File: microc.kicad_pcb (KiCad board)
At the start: 2 copper layers, 17.8 x 30.5 mm, 17 parts, among them J1 Conn_01x12, J2 Conn_01x12, J3 USB_C_Receptacle_USB2.0, U1 ATmega32U4-AU, U2 USBLC6-2SC6

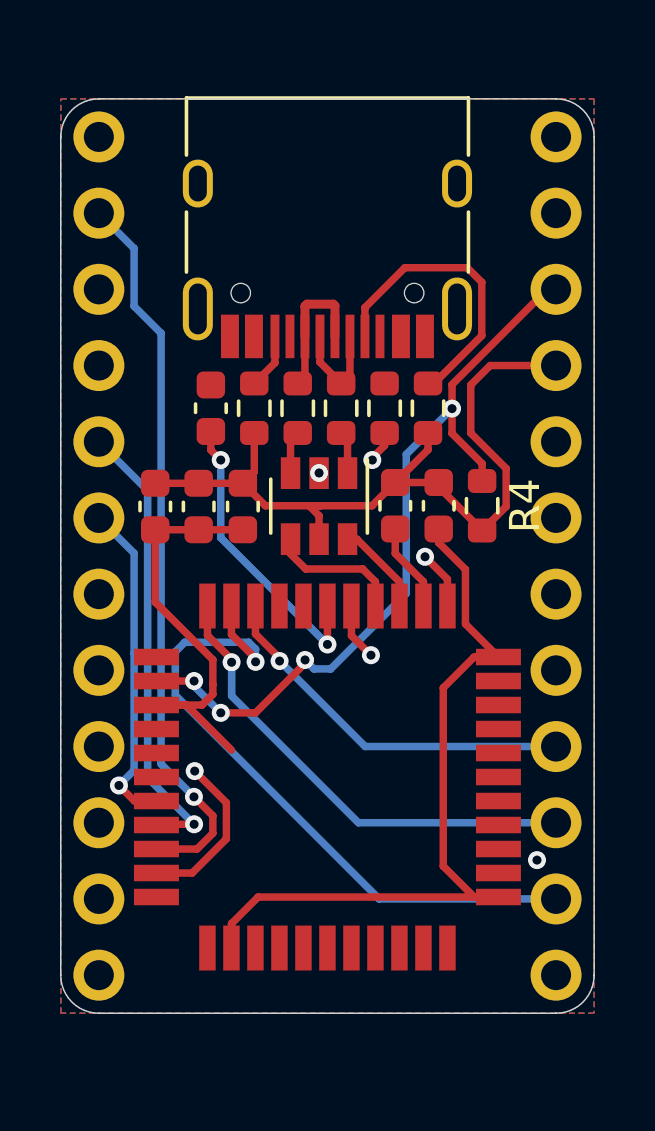
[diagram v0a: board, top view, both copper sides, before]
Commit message: rev 1 - Completed PCB - Completed schematic
Notes:
- Added 0 ohm resistor to schematic in order to help with routing
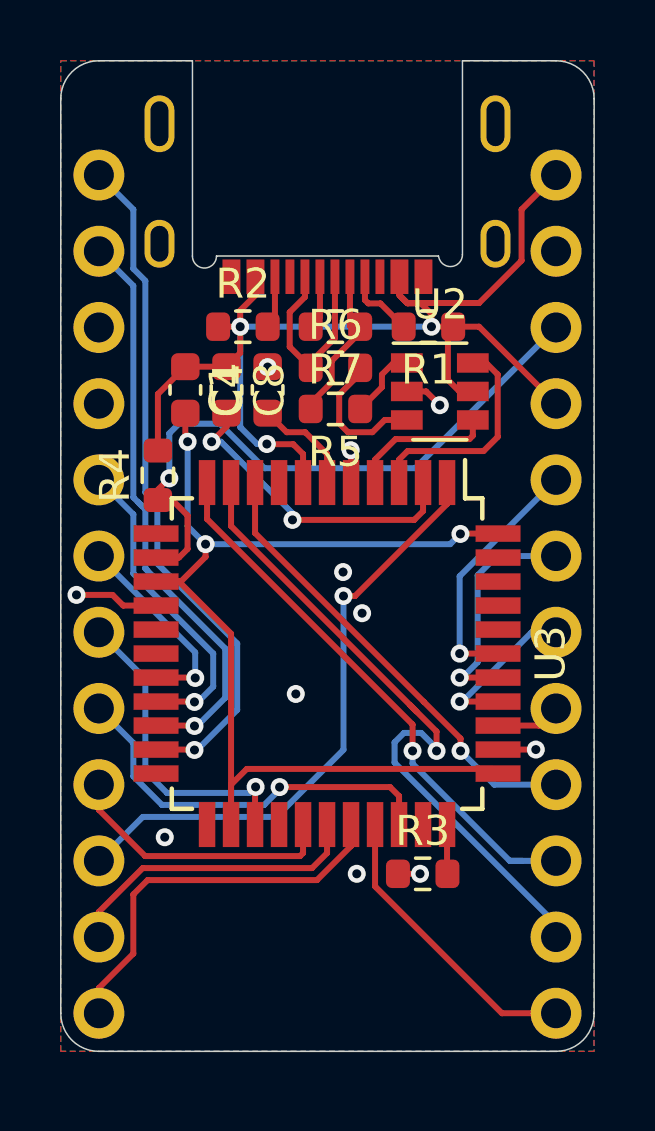
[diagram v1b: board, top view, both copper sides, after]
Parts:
- removed C5, C6, C7: 0.1u, Capacitor_SMD:C_0603_1608Metric
- removed U1: ATmega32U4-AU, Package_QFP:TQFP-44_10x10mm_P0.8mm
- added R7: 0, Resistor_SMD:R_0603_1608Metric, F.Cu at (150.3, 92.4)
- added U3: ATmega32U4RC-AU, Package_QFP:TQFP-44_10x10mm_P0.8mm, F.Cu at (150.0, 103.3)
- J3: footprint Connector_USB:USB_C_Receptacle_HRO_TYPE-C-31-M-12 -> kiboard:USB-C_16P_Midmount
- moved R3 15.6 mm to (153.2, 110.6), turned to 0 degrees
- moved R4 10.9 mm to (144.3, 97.3), turned to 90 degrees
- moved C8 6.82 mm to (146.6, 94.5)
- moved U2 5.55 mm to (153.7, 94.5), turned to 0 degrees
- moved J3 5.14 mm to (150.0, 83.5)
- moved C4 4.33 mm to (145.3, 94.5)
- moved R2 2.74 mm to (147.2, 92.4), turned to 0 degrees
- moved R1 2.72 mm to (153.4, 92.4), turned to 180 degrees
- moved C1 1.99 mm to (148.0, 94.5)
- moved R6 1.84 mm to (150.3, 93.7), turned to 0 degrees
- moved J1 1.27 mm to (142.4, 115.2)
- moved J2 1.27 mm to (157.6, 115.2)
- moved R5 0.19 mm to (150.3, 95.1), turned to 180 degrees
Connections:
- J3 pad B7: Net-(J3-PadA7) -> Net-(J3-PadB7)
- R5 pad 2: Net-(J3-PadA7) -> Net-(J3-PadB7)
- U2 pad 4: Net-(U1-Pad4) -> D+
- U2 pad 6: Net-(U1-Pad3) -> D-
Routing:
- net E6: track 1.95 -> 20.3 mm
- net D3: track 5.50 -> 23.0 mm
- net +5V: track 26.6 -> 40.4 mm, vias 0 -> 3
- net C6: track 0.00 -> 13.4 mm, vias 0 -> 1
- net B5: track 0.00 -> 13.1 mm
- net D4: track 0.00 -> 10.6 mm, vias 0 -> 1
- net B4: track 0.00 -> 10.2 mm
- net B6: track 0.00 -> 9.84 mm
- net D7: track 0.00 -> 9.28 mm
- net F4: track 0.00 -> 8.40 mm, vias 0 -> 1
- net F5: track 0.00 -> 7.87 mm, vias 0 -> 1
- net Net-(C8-Pad2): track 2.96 -> 10.5 mm, vias 0 -> 2
- net D-: track 0.00 -> 7.44 mm
- net Net-(J3-PadA5): track 9.84 -> 2.43 mm
- net Net-(C1-Pad1): track 9.99 -> 3.50 mm, vias 2 -> 0
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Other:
- board size 17.8 x 30.5 mm -> 17.8 x 33 mm
- net class Default: trace_width 0.25 -> 0.2

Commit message: rev1.1 - Added crystal to PCB
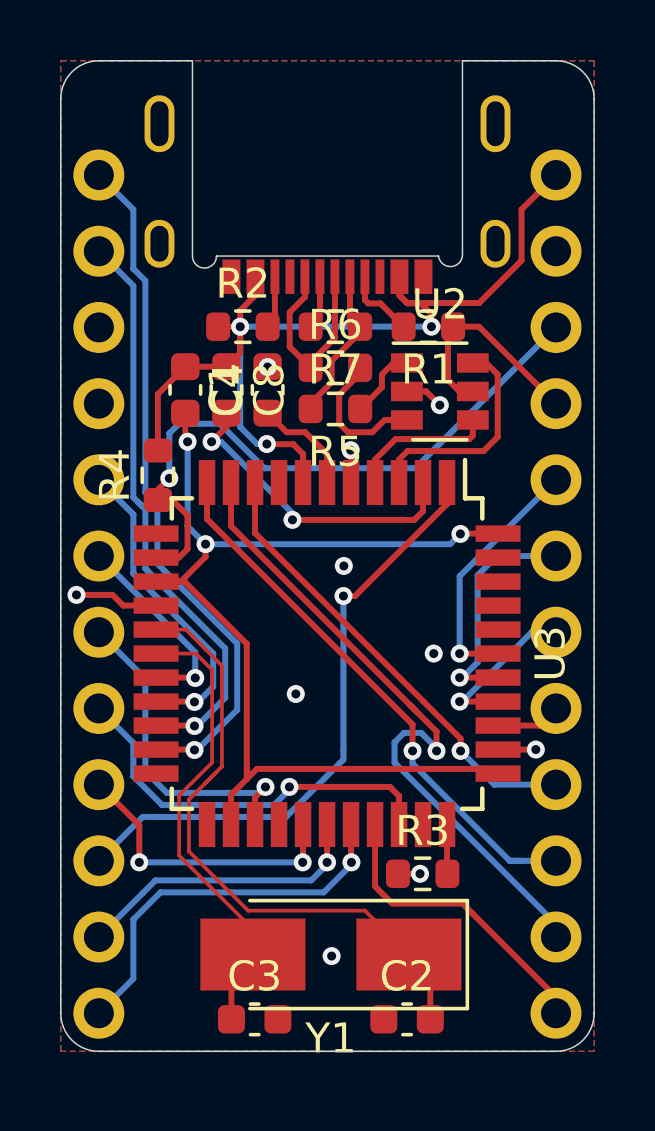
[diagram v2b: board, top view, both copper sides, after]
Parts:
- added C2: 22pf, Capacitor_SMD:C_0603_1608Metric, F.Cu at (152.7, 115.4)
- added C3: 22pf, Capacitor_SMD:C_0603_1608Metric, F.Cu at (147.6, 115.4)
- added Y1: 16mhz, Crystal:Crystal_SMD_5032-2Pin_5.0x3.2mm_HandSoldering, F.Cu at (150.1, 113.3)
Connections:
- net D+ renamed Net-(U2-Pad4)
- net D- renamed Net-(U2-Pad6)
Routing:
- net Net-(C2-Pad2): track 0.00 -> 21.1 mm
- net Net-(C3-Pad1): track 0.00 -> 15.5 mm
- net Net-(C4-Pad2): track 37.1 -> 35.7 mm
- net D7: track 9.28 -> 9.86 mm, vias 0 -> 2
- net B4: track 10.2 -> 9.94 mm, vias 0 -> 1
- net B5: track 13.1 -> 13.0 mm, vias 0 -> 1
- net GND: vias 11 -> 10

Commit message: rev1.2 - Removed 0 ohm resistor and replaced with via
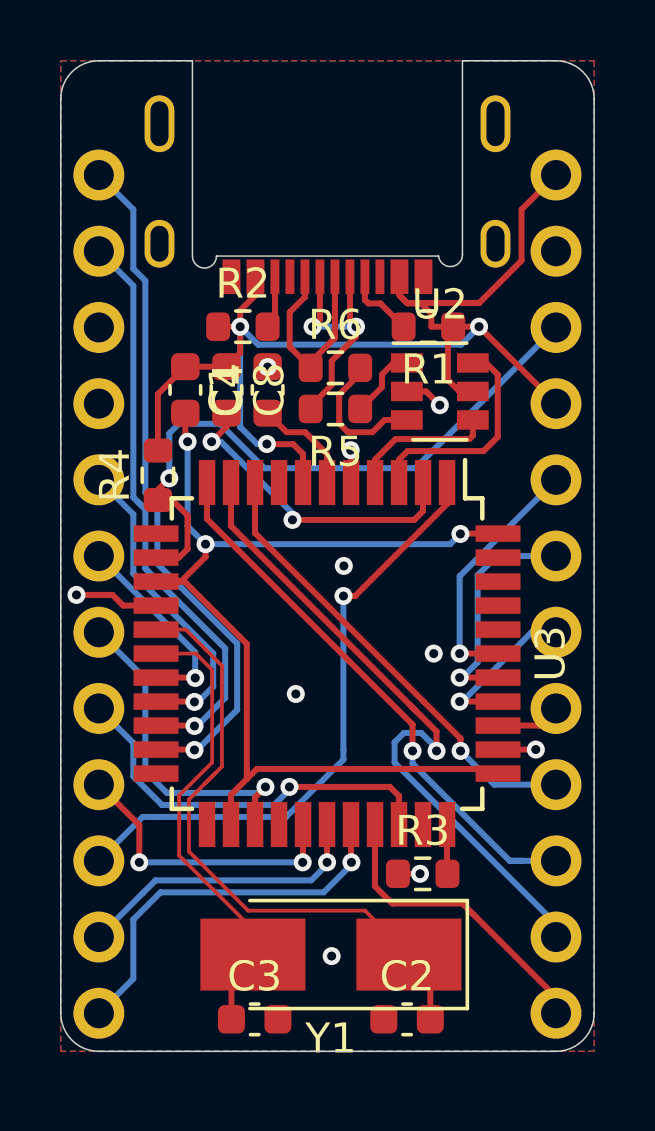
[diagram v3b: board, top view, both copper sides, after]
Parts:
- removed R7: 0, Resistor_SMD:R_0603_1608Metric
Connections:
- J3 pad B7: Net-(J3-PadB7) -> Net-(J3-PadA7)
- R5 pad 2: Net-(J3-PadB7) -> Net-(J3-PadA7)
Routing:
- net Net-(J3-PadA7): track 1.36 -> 8.33 mm, vias 0 -> 2
- net Net-(J3-PadB7): track 5.10 -> 0.00 mm
- net +5V: track 40.4 -> 42.5 mm

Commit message: rev1.2 - Aesthetic updates to PCB
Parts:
- moved R1 0.63 mm to (152.7, 92.4)
- moved R2 0.19 mm to (147.4, 92.4)
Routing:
- net Net-(C4-Pad2): track 35.7 -> 39.6 mm
- net B2: track 22.6 -> 25.8 mm
- net B1: track 15.4 -> 18.6 mm
- net RESET: track 21.5 -> 23.8 mm
- net B3: track 19.0 -> 20.7 mm
- net Net-(C8-Pad2): track 10.5 -> 11.6 mm
- net F5: track 7.87 -> 6.85 mm
- net +5V: track 42.5 -> 41.9 mm
- net GND: track 7.28 -> 7.93 mm, vias 10 -> 9

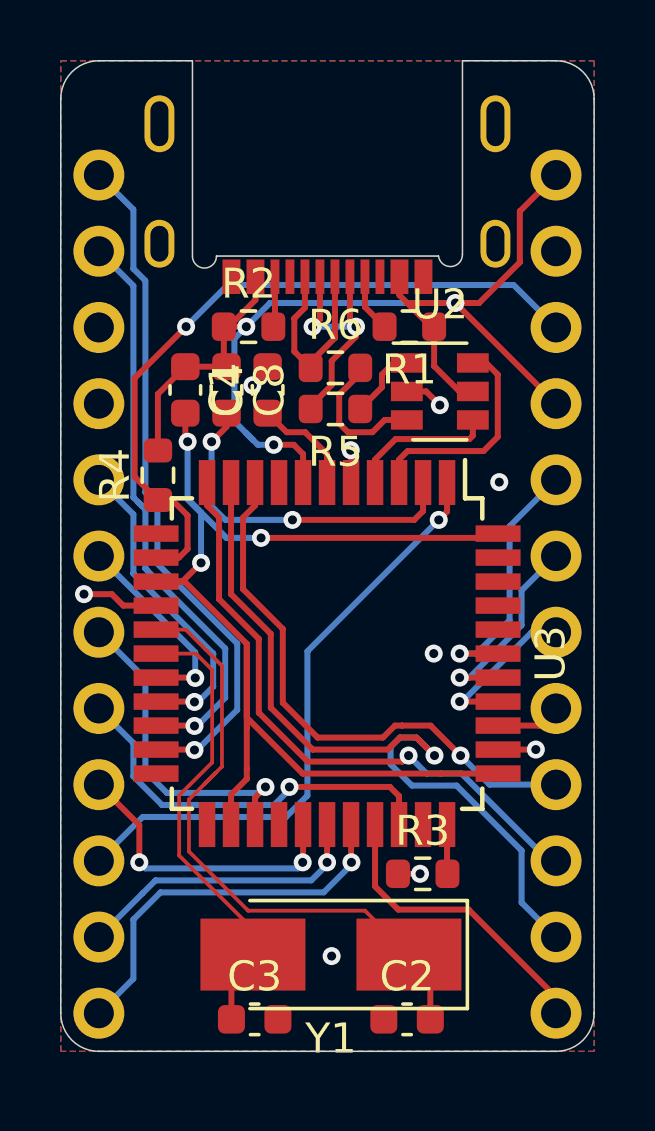
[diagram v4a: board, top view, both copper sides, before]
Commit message: rev 1.3 - Improved ground plane - Updated routing - Fixed error with power in schematic
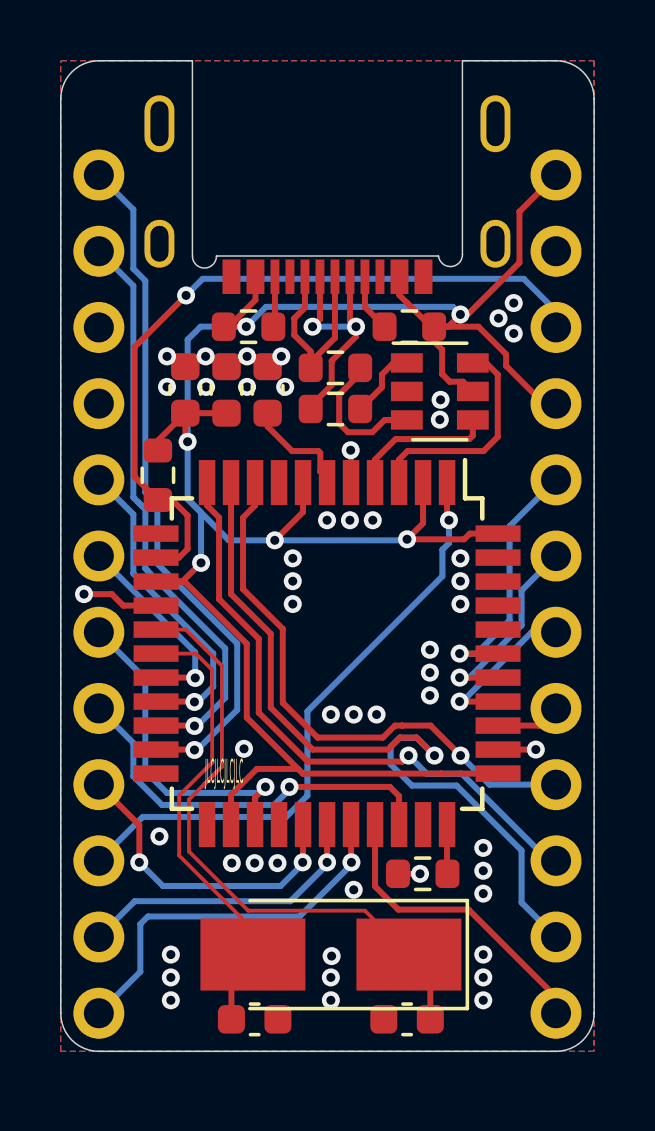
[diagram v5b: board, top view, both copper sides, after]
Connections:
- C4 pad 1: +5V -> GND
- C4 pad 2: Net-(C4-Pad2) -> +5V
- C8 pad 1: +5V -> GND
- C8 pad 2: Net-(C8-Pad2) -> +5V
- U3 pad 14: Net-(C4-Pad2) -> +5V
- U3 pad 2: Net-(C8-Pad2) -> +5V
- U3 pad 24: Net-(C4-Pad2) -> +5V
- U3 pad 34: Net-(C4-Pad2) -> +5V
- U3 pad 44: Net-(C4-Pad2) -> +5V
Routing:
- net Net-(C4-Pad2): track 39.6 -> 0.00 mm, vias 3 -> 0
- net +5V: track 41.9 -> 78.3 mm, vias 3 -> 6
- net Net-(C8-Pad2): track 11.6 -> 0.00 mm, vias 2 -> 0
- net GND: track 7.93 -> 5.74 mm, vias 9 -> 50
- net RESET: track 23.8 -> 24.9 mm
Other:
- board text added: "JLCJLCJLCJLC"
